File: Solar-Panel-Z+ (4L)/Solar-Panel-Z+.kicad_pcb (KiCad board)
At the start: 4 copper layers, 48.4 x 48.4 mm, 79 parts, among them J1 FTS-105-01-L-DV-A, Q1 BSS138DWQ-7, Q2 MBT2222ADW1T1, Q3 BSS138DWQ-7, Q4 MBT2222ADW1T1, U1 BQ25570RGRR, U2 TSL2561

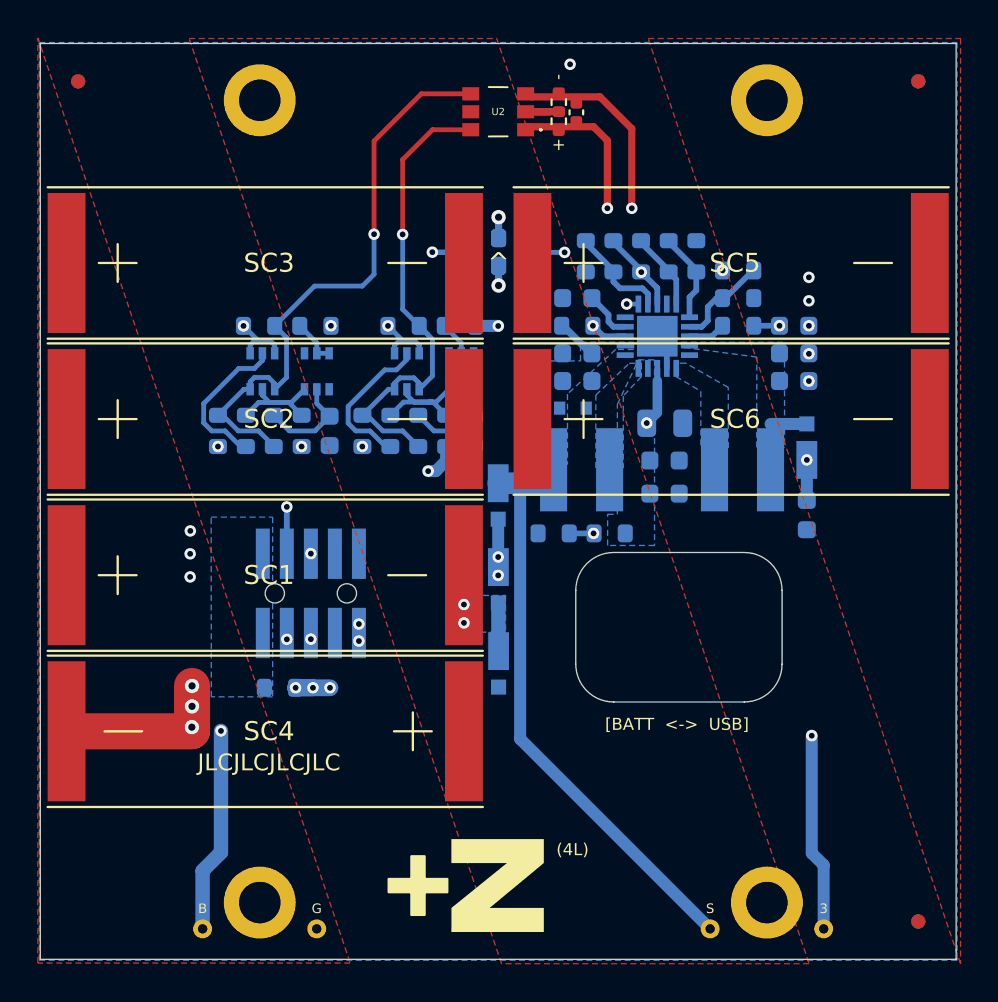
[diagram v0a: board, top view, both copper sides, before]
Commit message: Changed TSL2591 to BH1750
All boards (4L) except -Y
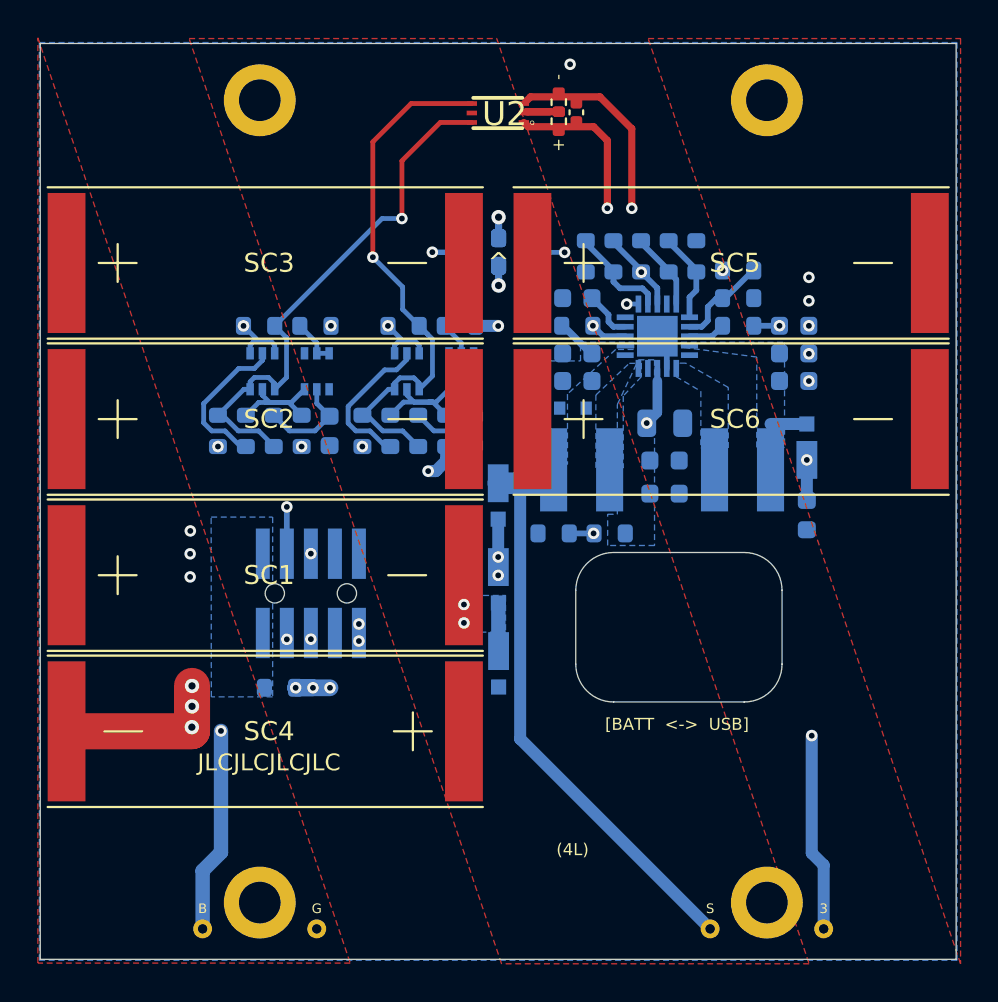
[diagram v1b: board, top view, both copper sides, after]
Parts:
- removed REF** (x6): Fiducial_0.75mm_Mask1.5mm, Fiducial:Fiducial_0.75mm_Mask1.5mm
- removed Ref**: Val**, custom-footprints:ypanel
- removed Ref**: Val**, custom-footprints:pycubed_mini_half
- U2: value TSL2561 -> BH1750FVI-TR; footprint solarpanels:TSL2561 -> solarpanels:WSOF6
- moved U2 0.07 mm to (106.7, 46.0)
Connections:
- R5 pad 1: Net-(R5-Pad1) -> Net-(R10-Pad2)
- R6 pad 2: Net-(R5-Pad1) -> Net-(R10-Pad2)
- U1 pad 7: Net-(R5-Pad1) -> Net-(R10-Pad2)
- U2 pad 4: SCL_LS -> SDA_LS
- U2 pad 6: SDA_LS -> SCL_LS
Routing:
- net Net-(R5-Pad1): track 5.21 -> 0.00 mm
- net Net-(R10-Pad2): track 8.44 -> 13.6 mm
- net SDA_LS: track 25.8 -> 29.2 mm
- net SCL_LS: track 31.3 -> 28.4 mm

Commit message: Updated light sensor to OPT 3001, Updated solar diodes.
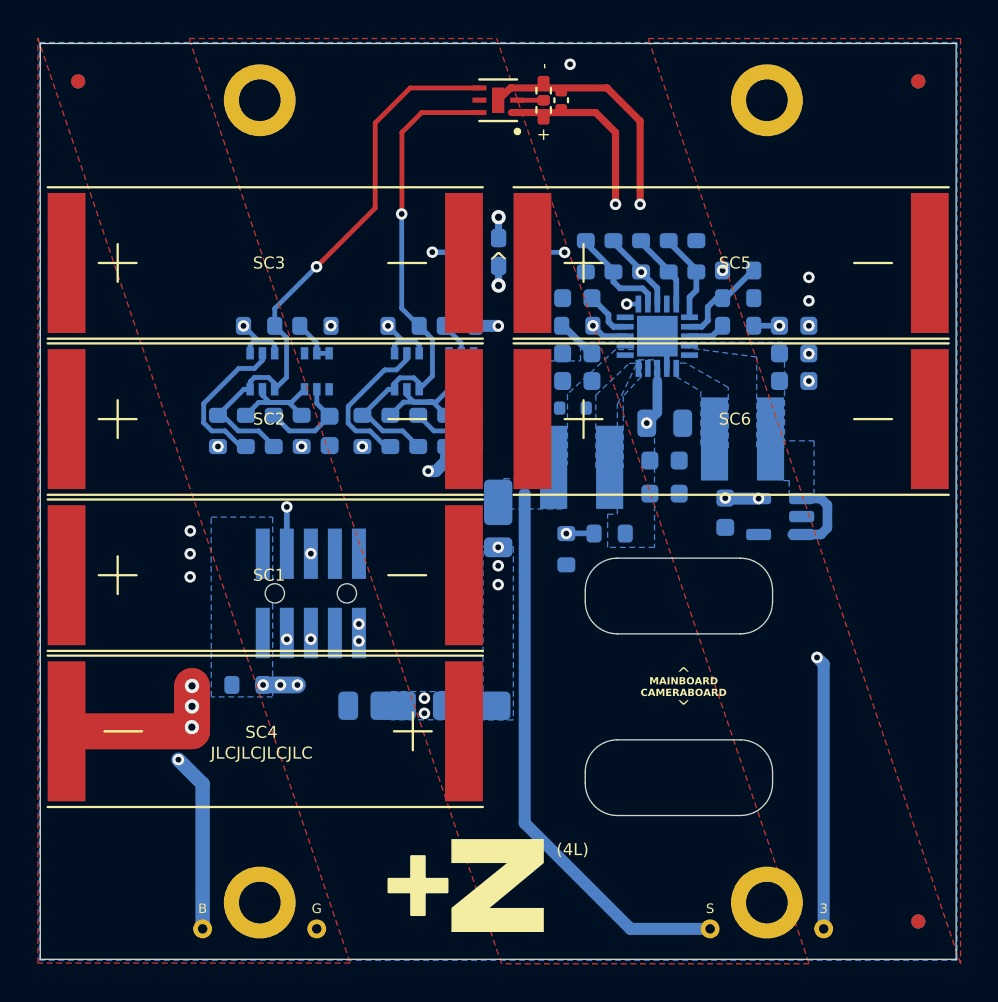
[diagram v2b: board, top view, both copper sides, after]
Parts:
- removed D5: MSS1P4-M3_89A, solarpanels:MICROSMP
- added REF**: Fiducial_0.75mm_Mask1.5mm, Fiducial:Fiducial_0.75mm_Mask1.5mm, F.Cu at (128.9, 88.7)
- added REF**: Fiducial_0.75mm_Mask1.5mm, Fiducial:Fiducial_0.75mm_Mask1.5mm, F.Cu at (84.5, 44.3)
- added REF**: Fiducial_0.75mm_Mask1.5mm, Fiducial:Fiducial_0.75mm_Mask1.5mm, F.Cu at (128.9, 44.3)
- added REF**: Fiducial_0.75mm_Mask1.5mm, Fiducial:Fiducial_0.75mm_Mask1.5mm, B.Cu at (128.9, 44.3)
- added REF**: Fiducial_0.75mm_Mask1.5mm, Fiducial:Fiducial_0.75mm_Mask1.5mm, B.Cu at (128.9, 88.7)
- added REF**: Fiducial_0.75mm_Mask1.5mm, Fiducial:Fiducial_0.75mm_Mask1.5mm, B.Cu at (84.5, 44.3)
- added Ref**: Val**, custom-footprints:ypanel, F.Cu at (106.0, 86.6)
- added Ref**: Val**, custom-footprints:pycubed_mini_half, B.Cu at (106.2, 44.5)
- added U3: MAX40200AUK, Package_TO_SOT_SMD:SOT-23-5, B.Cu at (121.6, 67.3)
- D2, D3, D4: value MSS1P4-M3_89A -> DFLS130L-7; footprint solarpanels:MICROSMP -> Diode_SMD:D_PowerDI-123
- J1: value FTS-105-01-L-DV-A -> FTS-105-01-X-DV-A
- Q1, Q3: value BSS138DWQ-7 -> NX3008NBKS
- R1, R12, R13, R16, R17, R18, R2, R3, R4: value 0 -> 0R
- R14, R15, R19, R20: value DNI -> DNI (0R)
- R21, R26: value 680 -> 680R
- U2: value BH1750FVI-TR -> OPT3001; footprint solarpanels:WSOF6 -> solarpanels:OPT3001
- moved D2 16.7 mm to (106.7, 67.4), turned to -90 degrees
- moved D4 6.83 mm to (105.3, 77.3), turned to 180 degrees
- moved D3 6.80 mm to (100.3, 77.3), turned to 180 degrees
- moved C11 4.31 mm to (118.7, 67.1)
- moved R3 1.73 mm to (93.5, 76.2)
- moved L2 1.63 mm to (119.6, 63.2)
- moved R15 1.07 mm to (110.3, 69.0), turned to 90 degrees
- moved C1 1.02 mm to (110.0, 45.3)
- moved R2 1.01 mm to (109.1, 44.8)
- moved R1 1.00 mm to (109.1, 45.8)
- moved U2 0.67 mm to (106.7, 45.3)
- moved L1 0.13 mm to (111.1, 64.7)
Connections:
- C10 pad 1: Net-(C10-Pad1) -> Net-(U1-VOUT)
- C8 pad 1: Net-(C10-Pad1) -> Net-(U1-VOUT)
- D2 pad 1: +3V3 -> VSOLAR
- D2 pad 2: Net-(C10-Pad1) -> /VSOLAR_FULL
- L2 pad 2: Net-(C10-Pad1) -> Net-(U1-VOUT)
- R10 pad 2: Net-(R10-Pad2) -> Net-(U1-VRDIV)
- R5 pad 1: Net-(R10-Pad2) -> Net-(U1-VBAT_OV)
- R5 pad 2: Net-(R10-Pad2) -> Net-(U1-VRDIV)
- R6 pad 2: Net-(R10-Pad2) -> Net-(U1-VBAT_OV)
- R7 pad 2: Net-(R10-Pad2) -> Net-(U1-VRDIV)
- U1 pad 14: Net-(C10-Pad1) -> Net-(U1-VOUT)
- U1 pad 7: Net-(R10-Pad2) -> Net-(U1-VBAT_OV)
- U1 pad 8: Net-(R10-Pad2) -> Net-(U1-VRDIV)
- U2 pad 4: SDA_LS -> SCL_LS
- U2 pad 6: SCL_LS -> SDA_LS
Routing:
- net /coil: track 6601.7 -> 6579.4 mm
- net Net-(R10-Pad2): track 13.6 -> 0.00 mm, vias 2 -> 0
- net Net-(U1-VRDIV): track 0.00 -> 8.44 mm, vias 0 -> 2
- net Net-(U1-VBAT_OV): track 0.00 -> 5.21 mm
- net +3V3: track 24.1 -> 29.1 mm, vias 11 -> 12
- net Net-(U1-VOUT): track 0.00 -> 4.71 mm
- net Net-(D3-K): track 2.54 -> 0.00 mm
- net SCL_LS: track 28.4 -> 30.9 mm
- net VBAT: track 16.9 -> 14.5 mm
- net GND: track 20.8 -> 23.1 mm
- net Net-(C10-Pad1): track 1.92 -> 0.00 mm
- net SDA_LS: track 29.2 -> 27.5 mm
- net Net-(U2-ADDR): track 2.96 -> 1.41 mm
- net VSOLAR: track 32.7 -> 31.6 mm
- net /VSOLAR_FULL: track 24.4 -> 23.3 mm, vias 5 -> 6
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- added copper zone on B.Cu, net /VSOLAR_FULL
- added copper zone on B.Cu, net Net-(U1-VOUT)
- removed copper zone on B.Cu, net Net-(C10-Pad1)
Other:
- outline, holes or cut-outs redrawn
- board text added: "MAINBOARD CAMERABOARD"
- board text added: "Rev B3/01"
- board text removed: "Rev B2/01"
- board text removed: "[BATT <-> USB]"

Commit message: Updated Mounting Holes
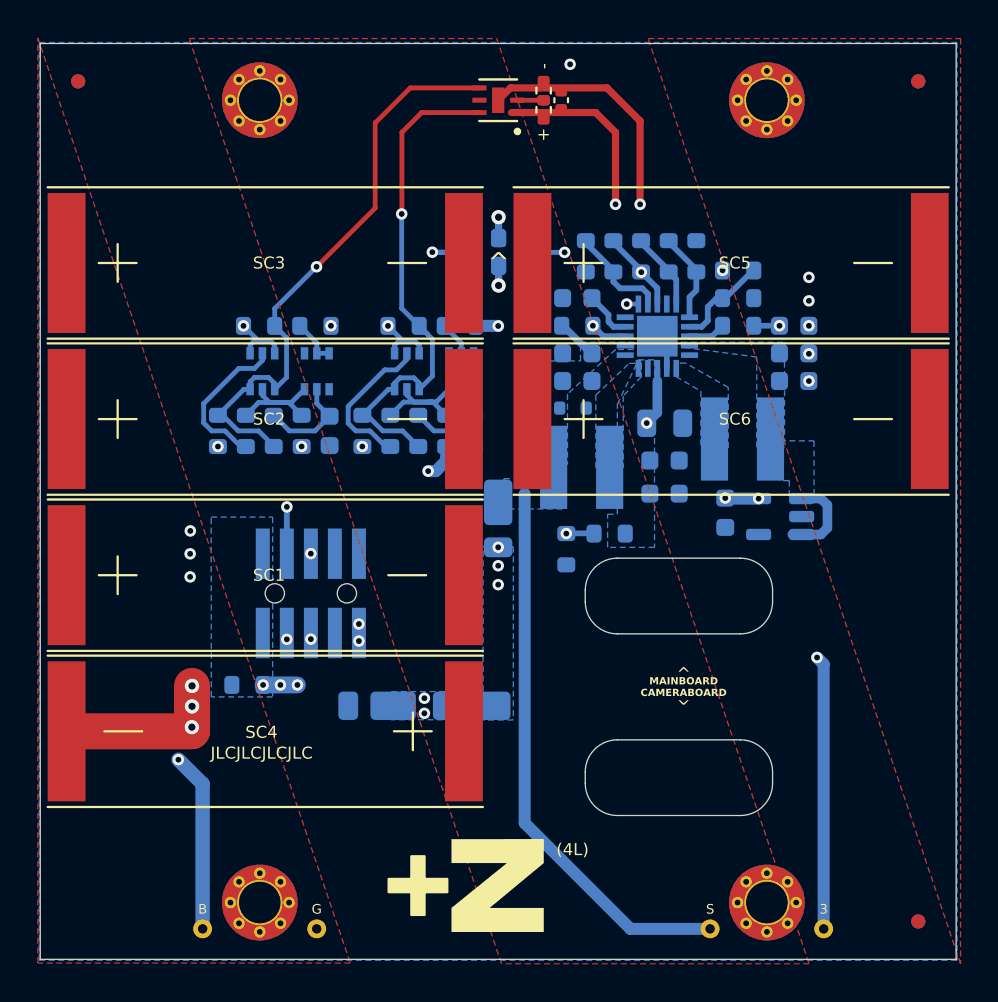
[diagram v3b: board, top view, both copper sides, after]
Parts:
- H1, H2, H3, H4: footprint MountingHole:MountingHole_2.2mm_M2_DIN965_Pad -> solarpanels:MountingHole_2.2mm_M2_DIN965_Pad_TopBottom; moved to F.Cu
- turned H1 to 0 degrees
- turned H2 to 0 degrees
- turned H3 to 0 degrees
- turned H4 to 0 degrees

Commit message: B3/02 Updates
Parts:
- C1: value 1uF -> 0.1uF
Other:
- board text added: "Rev B3/02"
- board text removed: "Rev B3/01"
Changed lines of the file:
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@@
     (39 "F.Mask" user)
     (40 "Dwgs.User" user "User.Drawings")
-    (41 "Cmts.User" user "User.Comments")
     (44 "Edge.Cuts" user)
     (45 "Margin" user)
@@
         (effects (font (size 0.381 0.381) (thickness 0.0762)))
     )
-    (fp_text value "1uF" (at 0 1.17 90) (layer "F.Fab")
+    (fp_text value "0.1uF" (at 0 1.17 90) (layer "F.Fab")
         (effects (font (size 1 1) (thickness 0.15)))
     )
@@
     (descr "Circular Fiducial, 0.75mm bare copper, 1.5mm soldermask opening (Level B)")
     (tags "fiducial")
-    (attr smd)
+    (attr smd exclude_from_bom)
     (fp_text reference "REF**" (at 0 -2) (layer "F.SilkS") hide
         (effects (font (size 1 1) (thickness 0.15)))
@@
     (property "Sheetfile" "Solar-Panel-Z+.kicad_sch")
     (property "Sheetname" "")
+    (property "exclude_from_bom" "")
     (property "ki_description" "Mounting Hole with connection")
     (property "ki_keywords" "mounting hole")
@@
     (fp_circle (center 0 0) (end 2.15 0)
       (stroke (width 0.05) (type solid)) (fill none) (layer "F.CrtYd"))
-    (pad "" np_thru_hole circle (at 0 0) (size 2.4 2.4) (drill 2.2) (layers "F&B.Cu" "*.Mask"))
+    (pad "" np_thru_hole circle (at 0 0) (size 2.4 2.4) (drill 2.2) (layers "*.Cu" "*.Mask"))
     (pad "1" thru_hole circle (at -1.55 0) (size 0.6096 0.6096) (drill 0.3048) (layers "*.Cu" "*.Mask")
       (net 1 "GND") (pinfunction "1") (pintype "input"))
@@
     (descr "Circular Fiducial, 0.75mm bare copper, 1.5mm soldermask opening (Level B)")
     (tags "fiducial")
-    (attr smd)
+    (attr smd exclude_from_bom)
     (fp_text reference "REF**" (at 0 -2) (layer "F.SilkS") hide
         (effects (font (size 1 1) (thickness 0.15)))
@@
     (descr "Circular Fiducial, 0.75mm bare copper, 1.5mm soldermask opening (Level B)")
     (tags "fiducial")
-    (attr smd)
+    (attr smd exclude_from_bom)
     (fp_text reference "REF**" (at 0 -2) (layer "F.SilkS") hide
         (effects (font (size 1 1) (thickness 0.15)))
@@
     (property "Sheetfile" "Solar-Panel-Z+.kicad_sch")
     (property "Sheetname" "")
+    (property "exclude_from_bom" "")
     (property "ki_description" "Mounting Hole with connection")
     (property "ki_keywords" "mounting hole")
@@
     (fp_circle (center 0 0) (end 2.15 0)
       (stroke (width 0.05) (type solid)) (fill none) (layer "F.CrtYd"))
-    (pad "" np_thru_hole circle (at 0 0) (size 2.4 2.4) (drill 2.2) (layers "F&B.Cu" "*.Mask"))
+    (pad "" np_thru_hole circle (at 0 0) (size 2.4 2.4) (drill 2.2) (layers "*.Cu" "*.Mask"))
     (pad "1" thru_hole circle (at -1.55 0) (size 0.6096 0.6096) (drill 0.3048) (layers "*.Cu" "*.Mask")
       (net 1 "GND") (pinfunction "1") (pintype "input"))
@@
   (footprint "custom-footprints:ypanel" (layer "F.Cu")
     (at 106.010401 86.552858)
-    (attr through_hole)
+    (attr through_hole exclude_from_bom)
     (fp_text reference "Ref**" (at -3.15 0.19) (layer "F.SilkS") hide
         (effects (font (size 1.27 1.27) (thickness 0.15)))
@@
     (property "Sheetfile" "Solar-Panel-Z+.kicad_sch")
     (property "Sheetname" "")
+    (property "exclude_from_bom" "")
     (property "ki_description" "Mounting Hole with connection")
     (property "ki_keywords" "mounting hole")
@@
     (fp_circle (center 0 0) (end 2.15 0)
       (stroke (width 0.05) (type solid)) (fill none) (layer "F.CrtYd"))
-    (pad "" np_thru_hole circle (at 0 0) (size 2.4 2.4) (drill 2.2) (layers "F&B.Cu" "*.Mask"))
+    (pad "" np_thru_hole circle (at 0 0) (size 2.4 2.4) (drill 2.2) (layers "*.Cu" "*.Mask"))
     (pad "1" thru_hole circle (at -1.55 0) (size 0.6096 0.6096) (drill 0.3048) (layers "*.Cu" "*.Mask")
       (net 1 "GND") (pinfunction "1") (pintype "input"))
@@
     (property "Sheetfile" "Solar-Panel-Z+.kicad_sch")
     (property "Sheetname" "")
+    (property "exclude_from_bom" "")
     (property "ki_description" "Mounting Hole with connection")
     (property "ki_keywords" "mounting hole")
@@
     (fp_circle (center 0 0) (end 2.15 0)
       (stroke (width 0.05) (type solid)) (fill none) (layer "F.CrtYd"))
-    (pad "" np_thru_hole circle (at 0 0) (size 2.4 2.4) (drill 2.2) (layers "F&B.Cu" "*.Mask"))
+    (pad "" np_thru_hole circle (at 0 0) (size 2.4 2.4) (drill 2.2) (layers "*.Cu" "*.Mask"))
     (pad "1" thru_hole circle (at -1.55 0) (size 0.6096 0.6096) (drill 0.3048) (layers "*.Cu" "*.Mask")
       (net 1 "GND") (pinfunction "1") (pintype "input"))
@@
     (property "Sheetfile" "Solar-Panel-Z+.kicad_sch")
     (property "Sheetname" "")
+    (property "exclude_from_bom" "")
     (property "ki_description" "test point")
     (property "ki_keywords" "test point tp")
-    (attr exclude_from_pos_files)
+    (attr exclude_from_pos_files exclude_from_bom)
     (fp_text reference "TP2" (at 0 1.448) (layer "B.SilkS") hide
         (effects (font (size 1 1) (thickness 0.15)) (justify mirror))
@@
     (property "Sheetfile" "Solar-Panel-Z+.kicad_sch")
     (property "Sheetname" "")
+    (property "exclude_from_bom" "")
     (property "ki_description" "test point")
     (property "ki_keywords" "test point tp")
-    (attr exclude_from_pos_files)
+    (attr exclude_from_pos_files exclude_from_bom)
     (fp_text reference "TP3" (at 0 1.448) (layer "B.SilkS") hide
         (effects (font (size 1 1) (thickness 0.15)) (justify mirror))
@@
     (property "Sheetfile" "Solar-Panel-Z+.kicad_sch")
     (property "Sheetname" "")
+    (property "exclude_from_bom" "")
     (property "ki_description" "test point")
     (property "ki_keywords" "test point tp")
-    (attr exclude_from_pos_files)
+    (attr exclude_from_pos_files exclude_from_bom)
     (fp_text reference "TP4" (at 0 1.448) (layer "B.SilkS") hide
         (effects (font (size 1 1) (thickness 0.15)) (justify mirror))
@@
     (property "Sheetfile" "Solar-Panel-Z+.kicad_sch")
     (property "Sheetname" "")
+    (property "exclude_from_bom" "")
     (property "ki_description" "test point")
     (property "ki_keywords" "test point tp")
-    (attr exclude_from_pos_files)
+    (attr exclude_from_pos_files exclude_from_bom)
     (fp_text reference "TP1" (at 0 1.448) (layer "B.SilkS") hide
         (effects (font (size 1 1) (thickness 0.15)) (justify mirror))
@@
     (descr "Circular Fiducial, 0.75mm bare copper, 1.5mm soldermask opening (Level B)")
     (tags "fiducial")
-    (attr smd)
+    (attr smd exclude_from_bom)
     (fp_text reference "REF**" (at 0 2) (layer "B.SilkS") hide
         (effects (font (size 1 1) (thickness 0.15)) (justify mirror))
@@
     (descr "Circular Fiducial, 0.75mm bare copper, 1.5mm soldermask opening (Level B)")
     (tags "fiducial")
-    (attr smd)
+    (attr smd exclude_from_bom)
     (fp_text reference "REF**" (at 0 2) (layer "B.SilkS") hide
         (effects (font (size 1 1) (thickness 0.15)) (justify mirror))
@@
     (descr "Circular Fiducial, 0.75mm bare copper, 1.5mm soldermask opening (Level B)")
     (tags "fiducial")
-    (attr smd)
+    (attr smd exclude_from_bom)
     (fp_text reference "REF**" (at 0 2) (layer "B.SilkS") hide
         (effects (font (size 1 1) (thickness 0.15)) (justify mirror))
@@
   (footprint "custom-footprints:pycubed_mini_half" (layer "B.Cu")
     (at 106.2 44.5 180)
-    (attr through_hole)
+    (attr through_hole exclude_from_bom)
     (fp_text reference "Ref**" (at 0 0) (layer "B.SilkS") hide
         (effects (font (size 1.27 1.27) (thickness 0.15)) (justify mirror))
@@
     (effects (font (size 0.508 0.508) (thickness 0.1016)))
   )
-  (gr_text "^" (at 116.5 76.9 180) (layer "F.SilkS")
-    (effects (font (size 0.635 0.635) (thickness 0.1016)))
+  (gr_text "^" (at 116.5 77.2 180) (layer "F.SilkS")
+    (effects (font (size 0.889 0.889) (thickness 0.127)))
   )
   (gr_text "MAINBOARD\nCAMERABOARD" (at 116.5 76.3) (layer "F.SilkS")
-    (effects (font (size 0.381 0.381) (thickness 0.0762) bold))
+    (effects (font (size 0.508 0.508) (thickness 0.1016) bold))
   )
   (gr_text "-" (at 109.1 43.5 90) (layer "F.SilkS")
@@
     (effects (font (size 0.508 0.508) (thickness 0.1016)))
   )
-  (gr_text "^" (at 116.5 75.6) (layer "F.SilkS")
-    (effects (font (size 0.635 0.635) (thickness 0.1016)))
+  (gr_text "^" (at 116.5 75.4) (layer "F.SilkS")
+    (effects (font (size 0.889 0.889) (thickness 0.127)))
   )
   (gr_text "S" (at 117.9 88.05) (layer "F.SilkS")
@@
     (effects (font (size 0.635 0.635) (thickness 0.127)))
   )
-  (gr_text "Rev B3/01" (at 105.825 46.665) (layer "B.Mask")
+  (gr_text "Rev B3/02" (at 105.825 46.665) (layer "B.Mask")
     (effects (font (size 0.635 0.635) (thickness 0.1524)) (justify mirror))
   )
